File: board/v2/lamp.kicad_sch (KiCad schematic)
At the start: 43 parts, among them J1 Conn_01x01_Female, J2 Conn_01x01_Female, J3 Conn_01x01_Female, J4 Conn_01x01_Female, J5 Conn_01x01_Female, J6 Conn_01x01_Female, J7 Conn_01x01_Female, J8 Conn_ARM_JTAG_SWD_10, Q1 SiA453EDJ, U1 STM32G071GxU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

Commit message: hardware: More wibbles
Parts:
- removed C2: 100n, Capacitor_SMD:C_0603_1608Metric, symbol Device:C
- D2: value D_Zener -> 5.1V; footprint Diode_SMD:D_SOD-323 -> Diode_SMD:D_SOD-123
- JP1: footprint Jumper:SolderJumper-2_P1.3mm_Bridged_Pad1.0x1.5mm -> Jumper:SolderJumper-2_P1.3mm_Bridged_RoundedPad1.0x1.5mm
- Q1: value SiA453EDJ -> SIA483DJ-T1-GE3‎; MFG (none) -> Vishay; MPN (none) -> SIA483DJ-T1-GE3‎
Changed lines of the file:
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@@
-    (pin "1")
-  )
-  (symbol (lib_name "power:+3.3V_1") (lib_id "power:+3.3V") (at 97.155 72.39 0) (unit 1)
-    (in_bom yes) (on_board yes)
-    (property "Reference" "#PWR05" (id 0) (at 97.155 76.2 0)
-      (effects (font (size 1.27 1.27)) hide)
-    )
-    (property "Value" "+3.3V" (id 1) (at 97.536 67.9958 0))
-    (property "Footprint" "" (id 2) (at 97.155 72.39 0)
-      (effects (font (size 1.27 1.27)) hide)
-    )
-    (property "Datasheet" "" (id 3) (at 97.155 72.39 0)
-      (effects (font (size 1.27 1.27)) hide)
-    )
     (pin "1")
   )
@@
     )
     (property "Datasheet" "" (id 3) (at 90.805 47.625 0)
-      (effects (font (size 1.27 1.27)) hide)
-    )
-    (pin "1")
-  )
-  (symbol (lib_name "power:GND_23") (lib_id "power:GND") (at 97.155 80.01 0) (unit 1)
-    (in_bom yes) (on_board yes)
-    (property "Reference" "#PWR06" (id 0) (at 97.155 86.36 0)
-      (effects (font (size 1.27 1.27)) hide)
-    )
-    (property "Value" "GND" (id 1) (at 97.282 84.4042 0))
-    (property "Footprint" "" (id 2) (at 97.155 80.01 0)
-      (effects (font (size 1.27 1.27)) hide)
-    )
-    (property "Datasheet" "" (id 3) (at 97.155 80.01 0)
       (effects (font (size 1.27 1.27)) hide)
     )
@@
     (property "Reference" "JP1" (id 0) (at -40.005 18.415 0))
     (property "Value" "Jumper_2_Bridged" (id 1) (at -40.005 20.955 0))
-    (property "Footprint" "Jumper:SolderJumper-2_P1.3mm_Bridged_Pad1.0x1.5mm" (id 2) (at -40.005 23.495 0)
+    (property "Footprint" "Jumper:SolderJumper-2_P1.3mm_Bridged_RoundedPad1.0x1.5mm" (id 2) (at -40.005 23.495 0)
       (effects (font (size 1.27 1.27)) hide)
     )
@@
   (symbol (lib_id "Device:D_Zener") (at -26.67 40.64 270) (unit 1)
     (in_bom yes) (on_board yes) (fields_autoplaced)
-    (property "Reference" "D2" (id 0) (at -23.495 40.0049 90)
-      (effects (font (size 1.27 1.27)) (justify left))
-    )
-    (property "Value" "D_Zener" (id 1) (at -23.495 42.5449 90)
-      (effects (font (size 1.27 1.27)) (justify left))
-    )
-    (property "Footprint" "Diode_SMD:D_SOD-323" (id 2) (at -26.67 40.64 0)
+    (property "Reference" "D2" (id 0) (at -22.86 40.0049 90)
+      (effects (font (size 1.27 1.27)) (justify left))
+    )
+    (property "Value" "5.1V" (id 1) (at -22.86 42.5449 90)
+      (effects (font (size 1.27 1.27)) (justify left))
+    )
+    (property "Footprint" "Diode_SMD:D_SOD-123" (id 2) (at -26.67 40.64 0)
       (effects (font (size 1.27 1.27)) hide)
     )
@@
     )
     (property "Datasheet" "~" (id 3) (at 85.725 76.2 0)
-      (effects (font (size 1.27 1.27)) hide)
-    )
-    (pin "1")
-    (pin "2")
-  )
-  (symbol (lib_id "Device:C") (at 97.155 76.2 0) (unit 1)
-    (in_bom yes) (on_board yes)
-    (property "Reference" "C2" (id 0) (at 100.076 75.0316 0)
-      (effects (font (size 1.27 1.27)) (justify left))
-    )
-    (property "Value" "100n" (id 1) (at 100.076 77.343 0)
-      (effects (font (size 1.27 1.27)) (justify left))
-    )
-    (property "Footprint" "Capacitor_SMD:C_0603_1608Metric" (id 2) (at 98.1202 80.01 0)
-      (effects (font (size 1.27 1.27)) hide)
-    )
-    (property "Datasheet" "~" (id 3) (at 97.155 76.2 0)
       (effects (font (size 1.27 1.27)) hide)
     )
@@
     (in_bom yes) (on_board yes) (fields_autoplaced)
     (property "Reference" "Q1" (id 0) (at -40.64 29.21 90))
-    (property "Value" "SiA453EDJ" (id 1) (at -40.64 31.75 90))
+    (property "Value" "SIA483DJ-T1-GE3‎" (id 1) (at -40.64 31.75 90))
     (property "Footprint" "Package_TO_SOT_SMD:Vishay_PowerPAK_SC70-6L_Single" (id 2) (at -38.735 33.02 0)
       (effects (font (size 1.27 1.27) italic) (justify left) hide)
@@
     (property "Datasheet" "http://www.vishay.com/docs/62864/sia453edj.pdf" (id 3) (at -40.64 38.1 90)
       (effects (font (size 1.27 1.27)) (justify left) hide)
+    )
+    (property "MFG" "Vishay" (id 4) (at -40.64 38.1 90)
+      (effects (font (size 1.27 1.27)) hide)
+    )
+    (property "MPN" "SIA483DJ-T1-GE3‎ " (id 5) (at -40.64 38.1 90)
+      (effects (font (size 1.27 1.27)) hide)
     )
     (pin "1")
@@
       (reference "#PWR04") (unit 1) (value "GND") (footprint "")
     )
-    (path "/00000000-0000-0000-0000-00005b39c3ba"
-      (reference "#PWR05") (unit 1) (value "+3.3V") (footprint "")
-    )
-    (path "/00000000-0000-0000-0000-00005b39c3c6"
-      (reference "#PWR06") (unit 1) (value "GND") (footprint "")
-    )
     (path "/00000000-0000-0000-0000-00005b36f592"
       (reference "#PWR010") (unit 1) (value "GND") (footprint "")
@@
       (reference "C1") (unit 1) (value "100n") (footprint "Capacitor_SMD:C_0603_1608Metric")
     )
-    (path "/00000000-0000-0000-0000-00005b39c3c0"
-      (reference "C2") (unit 1) (value "100n") (footprint "Capacitor_SMD:C_0603_1608Metric")
-    )
     (path "/00000000-0000-0000-0000-00005b41eebb"
       (reference "C4") (unit 1) (value "4.7u") (footprint "Capacitor_SMD:C_0603_1608Metric")
@@
     )
     (path "/8037ace0-5e49-4182-b38f-9fec37db3935"
-      (reference "D2") (unit 1) (value "D_Zener") (footprint "Diode_SMD:D_SOD-323")
+      (reference "D2") (unit 1) (value "5.1V") (footprint "Diode_SMD:D_SOD-123")
     )
     (path "/00000000-0000-0000-0000-00005b3bf396"
@@
     )
     (path "/dc1c9d5c-a713-4d7b-890b-8225bc61f3b8"
-      (reference "JP1") (unit 1) (value "Jumper_2_Bridged") (footprint "Jumper:SolderJumper-2_P1.3mm_Bridged_Pad1.0x1.5mm")
+      (reference "JP1") (unit 1) (value "Jumper_2_Bridged") (footprint "Jumper:SolderJumper-2_P1.3mm_Bridged_RoundedPad1.0x1.5mm")
     )
     (path "/00000000-0000-0000-0000-00005b36adf2"
@@
     )
     (path "/44d1900e-dcc8-4b4f-b07d-4ac91f439c84"
-      (reference "Q1") (unit 1) (value "SiA453EDJ") (footprint "Package_TO_SOT_SMD:Vishay_PowerPAK_SC70-6L_Single")
+      (reference "Q1") (unit 1) (value "SIA483DJ-T1-GE3‎") (footprint "Package_TO_SOT_SMD:Vishay_PowerPAK_SC70-6L_Single")
     )
     (path "/028a94a1-dcc1-4f16-84fd-d86ce7788415"

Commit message: board changes
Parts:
- JP1: value Jumper_2_Bridged -> Jumper_2_Open; footprint Jumper:SolderJumper-2_P1.3mm_Bridged_RoundedPad1.0x1.5mm -> Jumper:SolderJumper-2_P1.3mm_Open_RoundedPad1.0x1.5mm; symbol Jumper:Jumper_2_Bridged -> Jumper:Jumper_2_Open
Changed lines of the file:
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@@
-    (pin "2")
-  )
-  (symbol (lib_id "Jumper:Jumper_2_Bridged") (at -40.005 23.495 0) (unit 1)
-    (in_bom yes) (on_board yes) (fields_autoplaced)
-    (property "Reference" "JP1" (id 0) (at -40.005 18.415 0))
-    (property "Value" "Jumper_2_Bridged" (id 1) (at -40.005 20.955 0))
-    (property "Footprint" "Jumper:SolderJumper-2_P1.3mm_Bridged_RoundedPad1.0x1.5mm" (id 2) (at -40.005 23.495 0)
-      (effects (font (size 1.27 1.27)) hide)
-    )
-    (property "Datasheet" "~" (id 3) (at -40.005 23.495 0)
-      (effects (font (size 1.27 1.27)) hide)
-    )
-    (pin "1")
     (pin "2")
   )
@@
     )
     (property "Datasheet" "~" (id 3) (at -26.67 40.64 0)
+      (effects (font (size 1.27 1.27)) hide)
+    )
+    (pin "1")
+    (pin "2")
+  )
+  (symbol (lib_id "Jumper:Jumper_2_Open") (at -40.005 23.495 0) (unit 1)
+    (in_bom yes) (on_board yes) (fields_autoplaced)
+    (property "Reference" "JP1" (id 0) (at -40.005 18.415 0))
+    (property "Value" "Jumper_2_Open" (id 1) (at -40.005 20.955 0))
+    (property "Footprint" "Jumper:SolderJumper-2_P1.3mm_Open_RoundedPad1.0x1.5mm" (id 2) (at -40.005 23.495 0)
+      (effects (font (size 1.27 1.27)) hide)
+    )
+    (property "Datasheet" "~" (id 3) (at -40.005 23.495 0)
       (effects (font (size 1.27 1.27)) hide)
     )
@@
     )
     (path "/dc1c9d5c-a713-4d7b-890b-8225bc61f3b8"
-      (reference "JP1") (unit 1) (value "Jumper_2_Bridged") (footprint "Jumper:SolderJumper-2_P1.3mm_Bridged_RoundedPad1.0x1.5mm")
+      (reference "JP1") (unit 1) (value "Jumper_2_Open") (footprint "Jumper:SolderJumper-2_P1.3mm_Open_RoundedPad1.0x1.5mm")
     )
     (path "/00000000-0000-0000-0000-00005b36adf2"

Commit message: board: Update kicad
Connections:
- net ~RESET renamed ~{RESET}
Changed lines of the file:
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@@
-(kicad_sch (version 20210406) (generator eeschema)
+(kicad_sch (version 20210621) (generator eeschema)
   (paper "A4")
   (title_block
@@
     (effects (font (size 1.27 1.27)) (justify left bottom))
   )
-  (label "~RESET" (at 121.92 107.315 0)
-    (effects (font (size 1.27 1.27)) (justify left bottom))
-  )
+  (label "~{RESET}" (at 121.92 107.315 0)
+    (effects (font (size 1.27 1.27)) (justify left bottom))
+  )

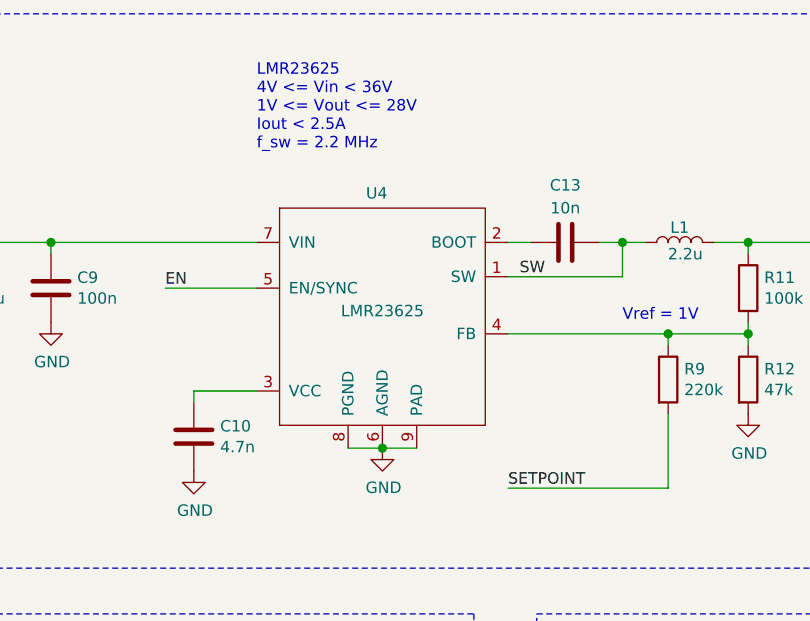
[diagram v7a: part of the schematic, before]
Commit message: board: Fix footprint of op-amp
The pinouts of the SC-70 and SOT-23-5 opamps are incompatible.
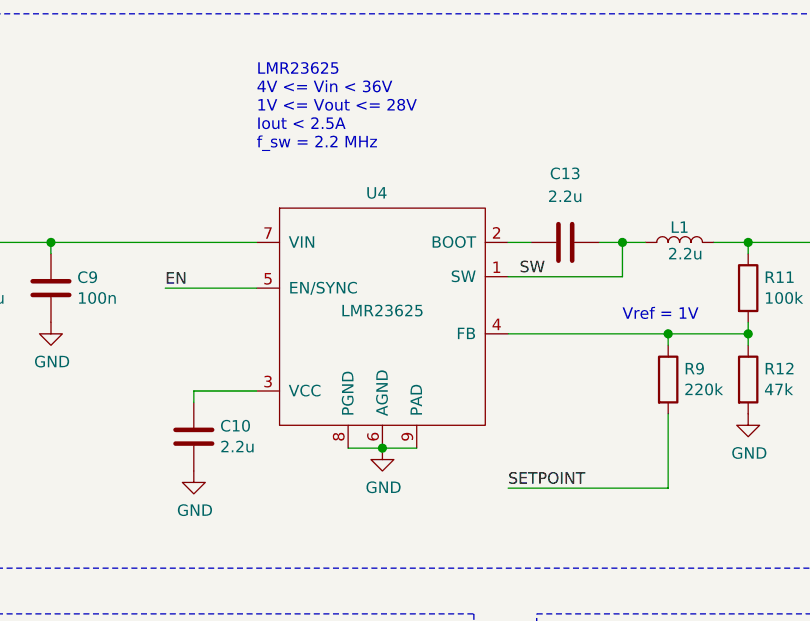
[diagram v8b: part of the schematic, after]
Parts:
- C10: value 4.7n -> 2.2u
- C13: value 10n -> 2.2u
- U2: footprint Package_TO_SOT_SMD:SOT-23-5 -> Package_TO_SOT_SMD:SOT-353_SC-70-5_Handsoldering
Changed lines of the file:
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@@
   (title_block
     (title "LED driver")
-    (date "2021-05-26")
-    (rev "4")
+    (date "2021-07-30")
+    (rev "5")
     (company "Ben Gamari")
   )
@@
       (effects (font (size 1.27 1.27)) (justify left))
     )
-    (property "Value" "4.7n" (id 1) (at 158.496 68.453 0)
+    (property "Value" "2.2u" (id 1) (at 158.496 68.453 0)
       (effects (font (size 1.27 1.27)) (justify left))
     )
@@
   (symbol (lib_id "Device:C") (at 196.85 45.72 90) (unit 1)
     (in_bom yes) (on_board yes) (fields_autoplaced)
-    (property "Reference" "C13" (id 0) (at 196.85 39.37 90))
-    (property "Value" "10n" (id 1) (at 196.85 41.91 90))
+    (property "Reference" "C13" (id 0) (at 196.85 38.1 90))
+    (property "Value" "2.2u" (id 1) (at 196.85 40.64 90))
     (property "Footprint" "Capacitor_SMD:C_0603_1608Metric" (id 2) (at 200.66 44.7548 0)
       (effects (font (size 1.27 1.27)) hide)
@@
     (property "Reference" "U2" (id 0) (at 239.395 100.33 0))
     (property "Value" "TLV333" (id 1) (at 237.49 102.87 0))
-    (property "Footprint" "Package_TO_SOT_SMD:SOT-23-5" (id 2) (at 242.57 106.68 0)
+    (property "Footprint" "Package_TO_SOT_SMD:SOT-353_SC-70-5_Handsoldering" (id 2) (at 242.57 106.68 0)
       (effects (font (size 1.27 1.27)) hide)
     )
@@
     )
     (path "/00000000-0000-0000-0000-00005b36b26c"
-      (reference "C10") (unit 1) (value "4.7n") (footprint "Capacitor_SMD:C_0603_1608Metric")
+      (reference "C10") (unit 1) (value "2.2u") (footprint "Capacitor_SMD:C_0603_1608Metric")
     )
     (path "/00000000-0000-0000-0000-00005b41c399"
@@
     )
     (path "/9eb5f14f-59d9-4d05-b707-8d55d9e6a286"
-      (reference "C13") (unit 1) (value "10n") (footprint "Capacitor_SMD:C_0603_1608Metric")
+      (reference "C13") (unit 1) (value "2.2u") (footprint "Capacitor_SMD:C_0603_1608Metric")
     )
     (path "/00000000-0000-0000-0000-00005b36b3cd"
@@
     )
     (path "/8a03bbc5-de75-4f92-b860-9775e48be713"
-      (reference "U2") (unit 1) (value "TLV333") (footprint "Package_TO_SOT_SMD:SOT-23-5")
+      (reference "U2") (unit 1) (value "TLV333") (footprint "Package_TO_SOT_SMD:SOT-353_SC-70-5_Handsoldering")
     )
     (path "/00000000-0000-0000-0000-00005b36da81"
